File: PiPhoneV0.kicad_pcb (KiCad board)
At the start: 2 copper layers, 70.5 x 115.3 mm, 50 parts, among them J1 GPIO, J2 Conn_01x40_MountingPin, J3 Conn_01x15_MountingPin, SW1 SW_Push, SW10 SW_Push, SW11 SW_Push, SW12 SW_Push, SW13 SW_Push, SW14 SW_Push, SW15 SW_Push, SW16 SW_Push, SW17 SW_Push, SW18 SW_Push, SW2 SW_Push, SW3 SW_Push, SW4 SW_Push, SW5 SW_Push, SW6 SW_Push, SW7 SW_Push, SW8 SW_Push, SW9 SW_Push, U1 ICN6211, U2 TPS61165DRV

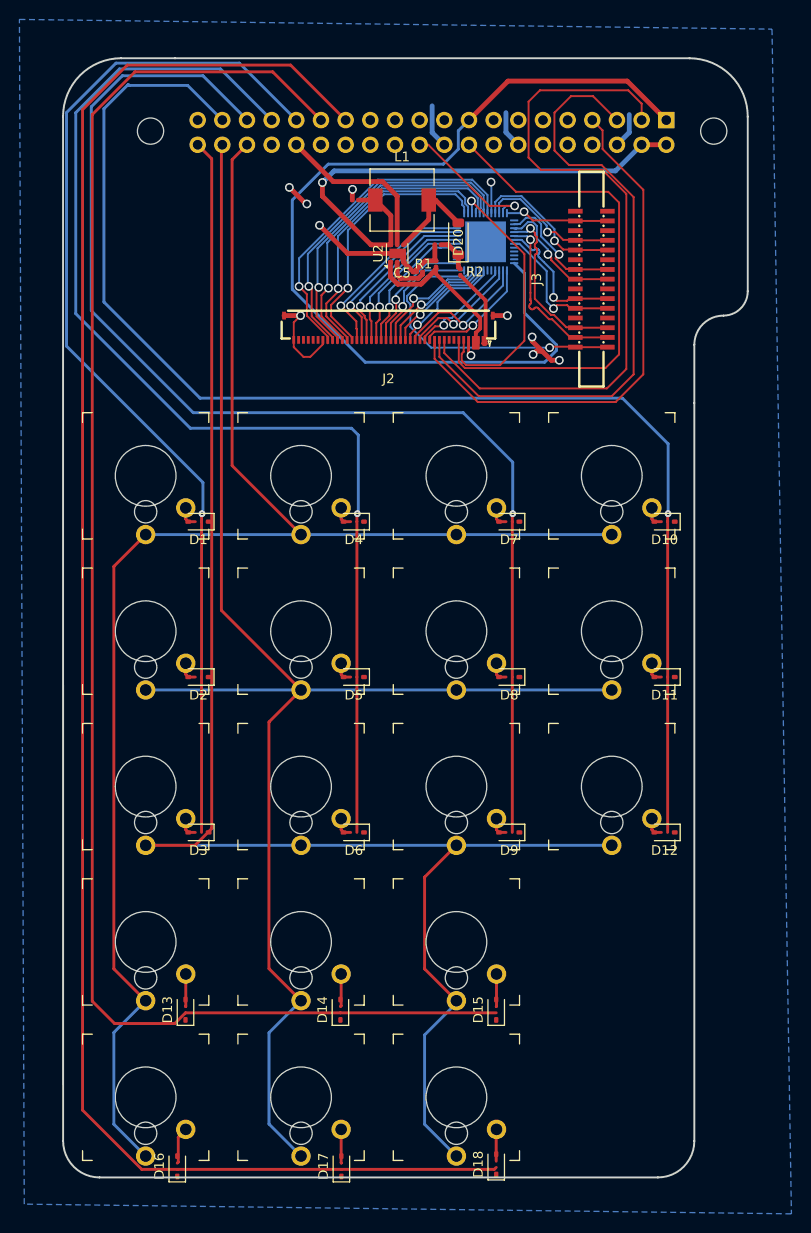
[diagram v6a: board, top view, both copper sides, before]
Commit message: chore: chill out drc a bit more
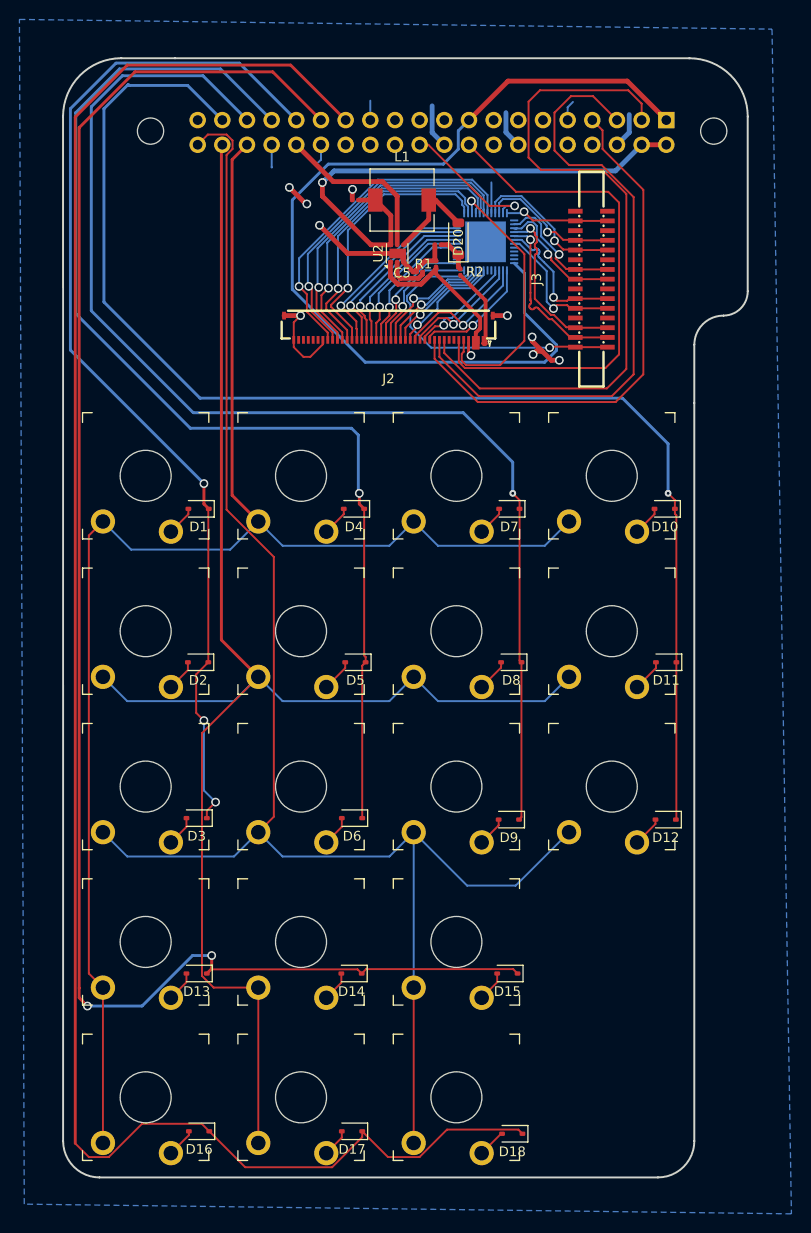
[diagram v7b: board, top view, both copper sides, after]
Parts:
- SW1, SW10, SW11, SW12, SW13, SW14, SW15, SW16, SW17, SW18, SW2, SW3, SW4, SW5, SW6, SW7, SW8, SW9: footprint 1 key-switches.pretty:SW_MX_LowProfile_THT -> 1 key-switches.pretty:SW_Gateron_LowProfile_THT
- moved D16 4.24 mm to (108.5, 199.5), turned to 180 degrees
- moved D13 3.90 mm to (108.2, 183.2), turned to 180 degrees
- moved D15 3.90 mm to (140.2, 183.2), turned to 180 degrees
- moved D14 3.90 mm to (124.2, 183.2), turned to 180 degrees
- moved D17 3.76 mm to (124.2, 199.5), turned to 180 degrees
- moved D18 3.56 mm to (140.8, 199.8), turned to 180 degrees
- moved D8 1.54 mm to (140.7, 151.2)
- moved D11 1.53 mm to (156.6, 151.2)
- moved D5 1.53 mm to (124.6, 151.2)
- moved D2 1.52 mm to (108.4, 151.2)
- moved D3 1.48 mm to (108.2, 167.2)
- moved D6 1.48 mm to (124.2, 167.2)
- moved D12 1.33 mm to (156.6, 167.4)
- moved D9 1.32 mm to (140.4, 167.4)
- moved D1 1.32 mm to (108.5, 135.4)
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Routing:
- net /ID_SDA: track 179.6 -> 192.3 mm
- net GND: track 52.0 -> 60.3 mm, vias 11 -> 10
- net /GPIO5: track 161.7 -> 169.9 mm, vias 0 -> 2
- net /GPIO20/PCM.DIN: track 161.0 -> 166.1 mm
- net /GPIO21/PCM.DOUT: track 164.0 -> 167.1 mm
- net /GPIO13/PWM1: track 120.4 -> 119.1 mm
- net Net-(D8-A): track 2.25 -> 3.38 mm
- net Net-(D11-A): track 2.25 -> 3.36 mm
- net Net-(D5-A): track 2.25 -> 3.36 mm
- net Net-(D2-A): track 2.25 -> 3.27 mm
- net /GPIO26: track 138.8 -> 137.9 mm
- net Net-(D16-A): track 3.98 -> 3.02 mm
- net Net-(D6-A): track 2.25 -> 3.16 mm
- net Net-(D3-A): track 2.25 -> 3.16 mm
- net Net-(D12-A): track 2.25 -> 3.14 mm
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
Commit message: feat: 3d models for everything!
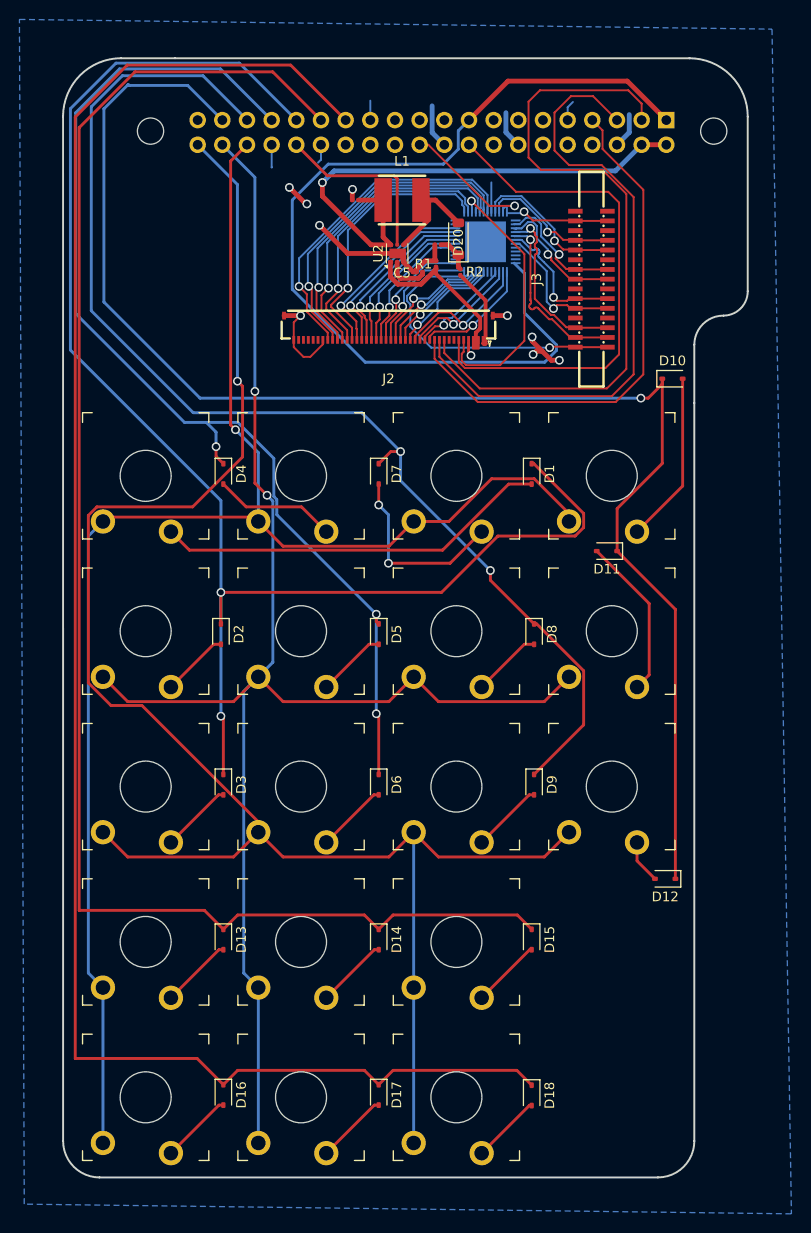
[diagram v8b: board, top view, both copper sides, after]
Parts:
- L1: footprint Inductor_SMD:L_6.3x6.3_H3 -> EasyEDA:IND-SMD_L5.0-W5.0-P3.60_SMNR5040
- U1: footprint Package_DFN_QFN:QFN-48-1EP_6x6mm_P0.4mm_EP4.2x4.2mm -> EasyEDA:QFN-48_L6.0-W6.0-P0.40-TL-EP4.2
- moved D1 34.5 mm to (142.8, 131.8), turned to -90 degrees
- moved D4 13.9 mm to (111.0, 131.8), turned to -90 degrees
- moved D7 13.9 mm to (127.0, 131.8), turned to -90 degrees
- moved D10 13.4 mm to (157.2, 122.0), turned to 0 degrees
- moved D11 13.0 mm to (150.5, 139.8)
- moved D12 6.10 mm to (156.5, 173.5)
- moved D17 4.65 mm to (127.0, 195.8), turned to -90 degrees
- moved D16 4.51 mm to (111.0, 195.8), turned to -90 degrees
- moved D14 4.48 mm to (127.0, 179.8), turned to -90 degrees
- moved D13 4.45 mm to (111.0, 179.8), turned to -90 degrees
- moved D9 4.44 mm to (143.0, 163.8), turned to -90 degrees
- moved D18 4.43 mm to (142.8, 195.8), turned to -90 degrees
- moved D3 4.41 mm to (111.0, 163.8), turned to -90 degrees
- moved D6 4.41 mm to (127.0, 163.8), turned to -90 degrees
- moved D15 4.30 mm to (142.8, 179.8), turned to -90 degrees
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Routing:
- net /GPIO6: track 108.3 -> 155.0 mm, vias 3 -> 2
- net Net-(D1-A): track 3.10 -> 40.8 mm
- net Net-(D7-A): track 3.10 -> 19.5 mm, vias 0 -> 2
- net /GPIO26: track 137.9 -> 153.3 mm
- net Net-(D10-A): track 3.10 -> 17.7 mm
- net Net-(D11-A): track 3.36 -> 16.8 mm
- net /GPIO21/PCM.DOUT: track 167.1 -> 180.5 mm, vias 0 -> 1
- net /ID_SDA: track 192.3 -> 179.9 mm
- net /GPIO5: track 169.9 -> 159.8 mm, vias 2 -> 0
- net Net-(D4-A): track 3.10 -> 12.6 mm
- net /GPIO20/PCM.DIN: track 166.1 -> 161.3 mm, vias 0 -> 2
- net Net-(D17-A): track 2.91 -> 7.45 mm
- net /GPIO13/PWM1: track 119.1 -> 114.6 mm, vias 1 -> 3
- net Net-(D16-A): track 3.02 -> 7.45 mm
- net Net-(D9-A): track 3.07 -> 7.43 mm
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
